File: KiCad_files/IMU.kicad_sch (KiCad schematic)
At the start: 1 part, among them U9 BNO055

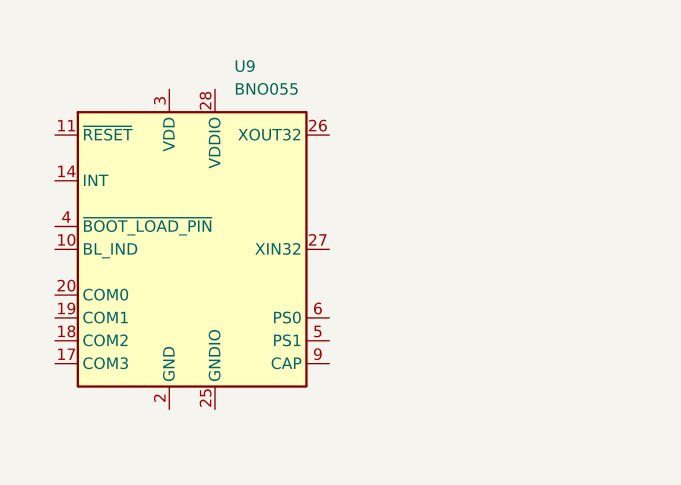
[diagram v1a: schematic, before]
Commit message: BNO085 lisätty kirjastoon
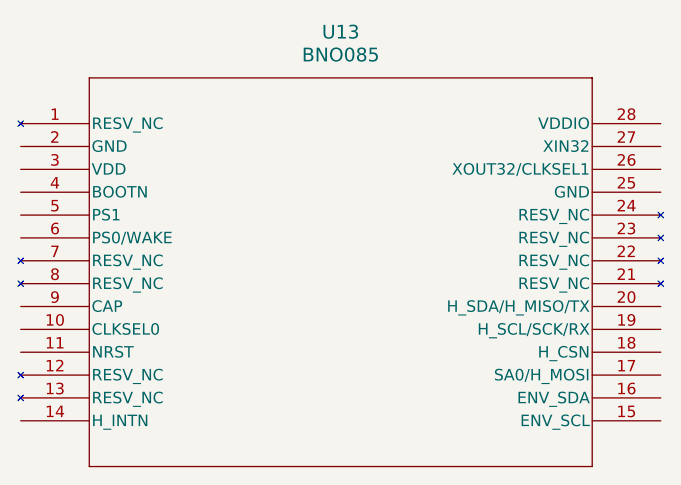
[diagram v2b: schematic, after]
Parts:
- removed U9: BNO055, Package_LGA:LGA-28_5.2x3.8mm_P0.5mm, symbol Sensor_Motion:BNO055
- added U13: BNO085, LGA-28_CEV, symbol 1_projektin osat:BNO085
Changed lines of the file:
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@@
 	(paper "A4")
 	(symbol
-		(lib_id "Sensor_Motion:BNO055")
-		(at 138.43 96.52 0)
+		(lib_id "1_projektin osat:BNO085")
+		(at 119.38 82.55 0)
 		(unit 1)
 		(exclude_from_sim no)
@@
 		(dnp no)
 		(fields_autoplaced yes)
-		(property "Reference" "U9"
-			(at 143.1133 76.2 0)
+		(property "Reference" "U13"
+			(at 154.94 72.39 0)
+			(effects
+				(font
+					(size 1.524 1.524)
+				)
+			)
+		)
+		(property "Value" "BNO085"
+			(at 154.94 74.93 0)
+			(effects
+				(font
+					(size 1.524 1.524)
+				)
+			)
+		)
+		(property "Footprint" "LGA-28_CEV"
+			(at 119.38 82.55 0)
 			(effects
 				(font
 					(size 1.27 1.27)
+					(italic yes)
 				)
-				(justify left)
+				(hide yes)
 			)
 		)
-		(property "Value" "BNO055"
-			(at 143.1133 78.74 0)
+		(property "Datasheet" "BNO085"
+			(at 119.38 82.55 0)
 			(effects
 				(font
 					(size 1.27 1.27)
+					(italic yes)
 				)
-				(justify left)
-			)
-		)
-		(property "Footprint" "Package_LGA:LGA-28_5.2x3.8mm_P0.5mm"
-			(at 144.78 113.03 0)
-			(effects
-				(font
-					(size 1.27 1.27)
-				)
-				(justify left)
 				(hide yes)
 			)
 		)
-		(property "Datasheet" "https://www.bosch-sensortec.com/media/boschsensortec/downloads/datasheets/bst-bno055-ds000.pdf"
-			(at 138.43 91.44 0)
+		(property "Description" ""
+			(at 119.38 82.55 0)
 			(effects
 				(font
@@
 			)
 		)
-		(property "Description" "Intelligent 9-axis absolute orientation sensor, LGA-28"
-			(at 138.43 96.52 0)
-			(effects
-				(font
-					(size 1.27 1.27)
-				)
-				(hide yes)
-			)
+		(pin "2"
+		)
+		(pin "1"
+		)
+		(pin "11"
+		)
+		(pin "28"
+		)
+		(pin "6"
+		)
+		(pin "4"
+		)
+		(pin "13"
 		)
 		(pin "14"
 		)
+		(pin "25"
+		)
+		(pin "5"
+		)
+		(pin "3"
+		)
+		(pin "7"
+		)
+		(pin "8"
+		)
+		(pin "9"
+		)
 		(pin "10"
 		)
-		(pin "25"
+		(pin "12"
 		)
-		(pin "11"
+		(pin "27"
 		)
-		(pin "4"
+		(pin "23"
+		)
+		(pin "24"
+		)
+		(pin "26"
+		)
+		(pin "22"
+		)
+		(pin "21"
 		)
 		(pin "20"
 		)
-		(pin "19"
+		(pin "16"
 		)
 		(pin "17"
 		)
-		(pin "1"
-		)
-		(pin "7"
-		)
-		(pin "3"
-		)
-		(pin "2"
-		)
-		(pin "8"
+		(pin "19"
 		)
 		(pin "18"
 		)
-		(pin "28"
-		)
-		(pin "9"
-		)
-		(pin "21"
-		)
-		(pin "5"
-		)
-		(pin "27"
-		)
-		(pin "26"
-		)
-		(pin "12"
-		)
-		(pin "22"
-		)
 		(pin "15"
 		)
-		(pin "6"
-		)
-		(pin "24"
-		)
-		(pin "13"
-		)
-		(pin "23"
-		)
-		(pin "16"
-		)
 		(instances
-			(project "esp"
+			(project ""
 				(path "/186d5500-054c-4b47-a89c-85f6ce2abe33/1d098c74-ef64-49cb-a95a-ee89cc8acd66"
-					(reference "U9")
+					(reference "U13")
 					(unit 1)
 				)

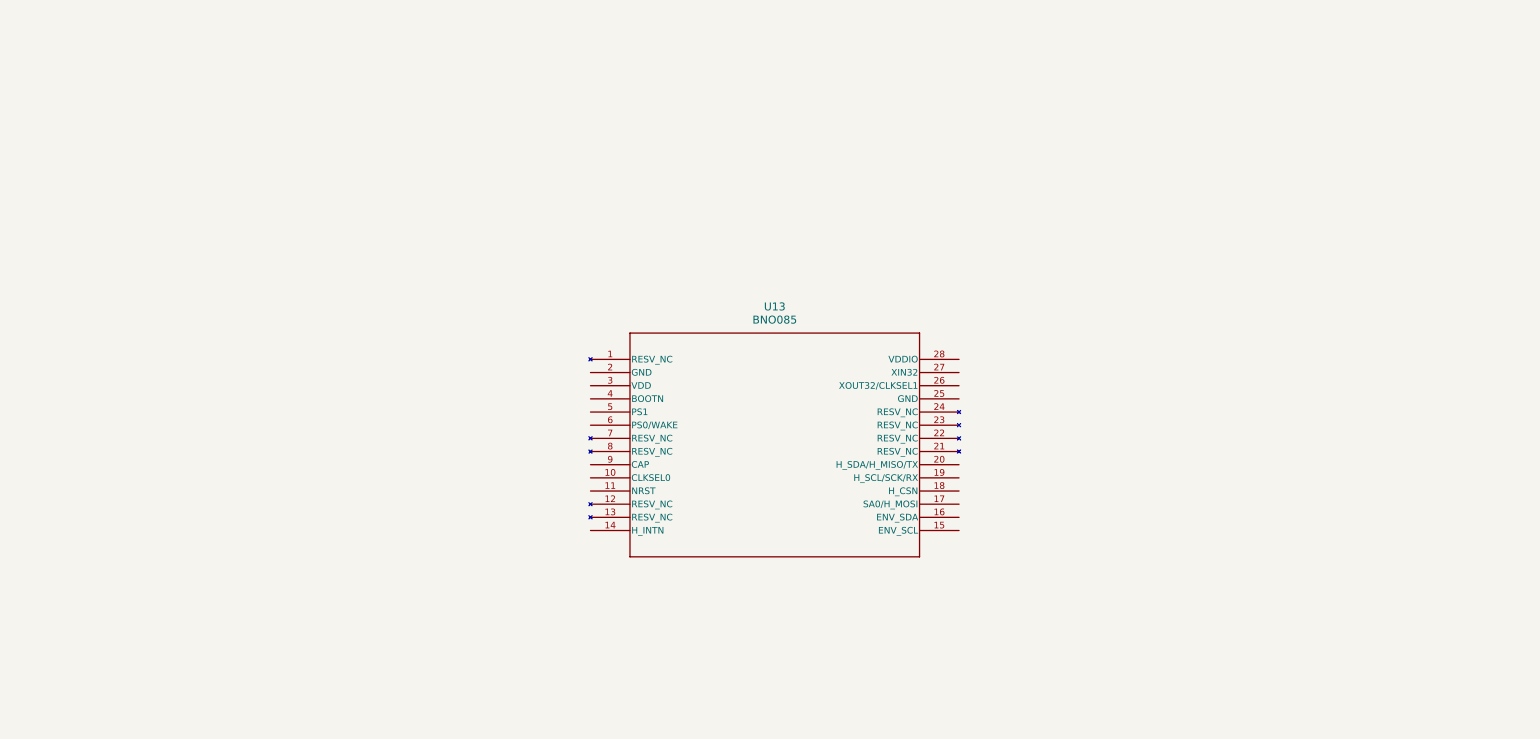
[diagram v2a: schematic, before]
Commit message: IMU schematic drawn
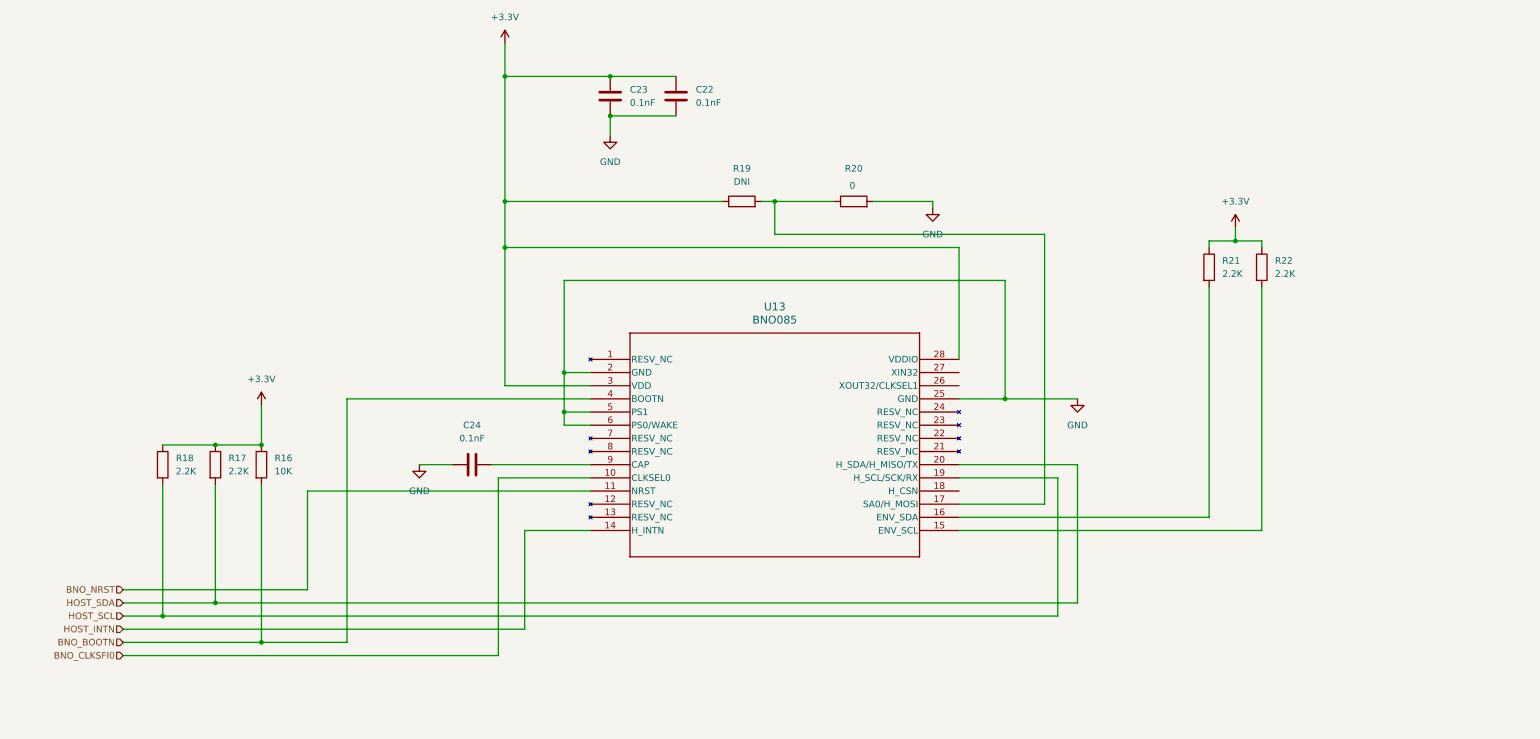
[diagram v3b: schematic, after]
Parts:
- added C22, C23, C24: 0.1nF, symbol Device:C
- added R16: 10K, symbol Device:R
- added R17, R18, R21, R22: 2.2K, symbol Device:R
- added R19: DNI, symbol Device:R
- added R20: 0, symbol Device:R
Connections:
- net BNO_CLKSFI0: now reaches U13.10 (CLKSEL0)
- net BNO_NRST: now reaches U13.11 (NRST)
- net HOST_INTN: now reaches U13.14 (H_INTN)
- net at U13.15 (ENV_SCL): now also R22.2
- net at U13.16 (ENV_SDA): now also R21.2
- net at U13.17 (SA0/H_MOSI): now also R19.2, R20.1
- net HOST_SCL: now reaches U13.19 (H_SCL/SCK/RX)
- net HOST_SCL: now also R18.2
- net GND: now reaches U13.2 (GND)
- net GND: now also U13.25 (GND), U13.5 (PS1), U13.6 (PS0/WAKE), C22.2, C23.2, C24.2, R20.2
- net HOST_SDA: now reaches U13.20 (H_SDA/H_MISO/TX)
- net HOST_SDA: now also R17.2
- net +3.3V: now reaches U13.28 (VDDIO)
- net +3.3V: now also U13.3 (VDD), C22.1, C23.1, R16.1, R17.1, R18.1, R19.1, R21.1, R22.1
- net BNO_BOOTN: now reaches U13.4 (BOOTN)
- net BNO_BOOTN: now also R16.2
- net at U13.9 (CAP): now also C24.1

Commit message: tekstiä
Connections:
- net HOST_INTN is gone; now on net BNO_BOOTN: U13.14 (H_INTN)
- net HOST_SDA is gone; now on net HOST_SCL: R17.2, U13.20 (H_SDA/H_MISO/TX)
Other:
- note added: "The BNO08X I2C interface answers to a 7-bit address of either 0x4A or 0x4B"
- note added: "i2c clock line"
- note added: "i2c data line"
- note added: "if bootn is low when reset, enter bootloader"
- note added: "interrupt line, connect to gpio with wake up capability, interrupt is active when low"
- note added: "optional secondary sensors require pulling i2c up regaardless of their presence"
- note added: "pin17 can be used to select lower bit of i2c slave address, no idea what that means"
- note added: "ps0 and ps1 are pulled to ground to select i2c"
- note added: "reset line, drive from processor or board reset"
- note added: "set lowest bit of the slave address, either low or high depending on setup"
- moved on the sheet: R21, R22

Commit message: mohloilut korjattu
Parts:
- added R23: 10K, symbol Device:R
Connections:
- net +3.3V: now also R23.1
- net BNO_BOOTN: no longer U13.14 (H_INTN)
- net BNO_CLKSFI0: now also R23.2
- net GND: now also U13.26 (XOUT32/CLKSEL1)
- net HOST_SCL: no longer R18.2, U13.20 (H_SDA/H_MISO/TX)
- new net HOST_INTN: U13.14 (H_INTN)
- new net HOST_SDA: R18.2, U13.20 (H_SDA/H_MISO/TX)
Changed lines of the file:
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@@
 	)
 	(junction
-		(at 46.99 132.08)
+		(at 55.88 147.32)
 		(diameter 0)
 		(color 0 0 0 0)
@@
 	)
 	(junction
-		(at 46.99 129.54)
-		(diameter 0)
-		(color 0 0 0 0)
-	)
-	(junction
-		(at 55.88 142.24)
-		(diameter 0)
-		(color 0 0 0 0)
-	)
-	(junction
 		(at 114.3 92.71)
 		(diameter 0)
@@
 	)
 	(junction
+		(at 46.99 137.16)
+		(diameter 0)
+		(color 0 0 0 0)
+	)
+	(junction
 		(at 36.83 132.08)
 		(diameter 0)
@@
 	)
 	(junction
-		(at 72.39 137.16)
-		(diameter 0)
-		(color 0 0 0 0)
-	)
-	(junction
 		(at 102.87 27.94)
 		(diameter 0)
@@
 	)
 	(junction
+		(at 55.88 95.25)
+		(diameter 0)
+		(color 0 0 0 0)
+	)
+	(junction
 		(at 102.87 60.96)
 		(diameter 0)
@@
 	)
 	(junction
+		(at 195.58 90.17)
+		(diameter 0)
+		(color 0 0 0 0)
+	)
+	(junction
+		(at 69.85 152.4)
+		(diameter 0)
+		(color 0 0 0 0)
+	)
+	(junction
 		(at 123.19 27.94)
 		(diameter 0)
@@
 	)
 	(junction
-		(at 55.88 137.16)
-		(diameter 0)
-		(color 0 0 0 0)
-	)
-	(junction
 		(at 243.84 100.33)
 		(diameter 0)
@@
 	(wire
 		(pts
-			(xy 46.99 129.54) (xy 213.36 129.54)
-		)
-		(stroke
-			(width 0)
-			(type default)
-		)
-	)
-	(wire
-		(pts
 			(xy 64.77 107.95) (xy 119.38 107.95)
 		)
@@
 	(wire
 		(pts
-			(xy 46.99 132.08) (xy 209.55 132.08)
+			(xy 119.38 115.57) (xy 119.38 142.24)
 		)
 		(stroke
@@
 	(wire
 		(pts
+			(xy 204.47 102.87) (xy 204.47 132.08)
+		)
+		(stroke
+			(width 0)
+			(type default)
+		)
+	)
+	(wire
+		(pts
 			(xy 207.01 110.49) (xy 190.5 110.49)
 		)
@@
 	(wire
 		(pts
+			(xy 195.58 90.17) (xy 199.39 90.17)
+		)
+		(stroke
+			(width 0)
+			(type default)
+		)
+	)
+	(wire
+		(pts
 			(xy 248.92 100.33) (xy 243.84 100.33)
 		)
@@
 	(wire
 		(pts
-			(xy 72.39 137.16) (xy 106.68 137.16)
-		)
-		(stroke
-			(width 0)
-			(type default)
-		)
-	)
-	(wire
-		(pts
 			(xy 114.3 67.31) (xy 199.39 67.31)
 		)
@@
 	(wire
 		(pts
-			(xy 55.88 91.44) (xy 55.88 99.06)
+			(xy 55.88 91.44) (xy 55.88 95.25)
 		)
 		(stroke
@@
 	(wire
 		(pts
-			(xy 36.83 132.08) (xy 46.99 132.08)
-		)
-		(stroke
-			(width 0)
-			(type default)
-		)
-	)
-	(wire
-		(pts
-			(xy 29.21 137.16) (xy 36.83 137.16)
+			(xy 55.88 106.68) (xy 55.88 147.32)
+		)
+		(stroke
+			(width 0)
+			(type default)
+		)
+	)
+	(wire
+		(pts
+			(xy 36.83 132.08) (xy 204.47 132.08)
+		)
+		(stroke
+			(width 0)
+			(type default)
+		)
+	)
+	(wire
+		(pts
+			(xy 29.21 137.16) (xy 46.99 137.16)
+		)
+		(stroke
+			(width 0)
+			(type default)
+		)
+	)
+	(wire
+		(pts
+			(xy 72.39 147.32) (xy 72.39 90.17)
 		)
 		(stroke
@@
 	(wire
 		(pts
-			(xy 106.68 115.57) (xy 119.38 115.57)
-		)
-		(stroke
-			(width 0)
-			(type default)
-		)
-	)
-	(wire
-		(pts
 			(xy 114.3 92.71) (xy 114.3 85.09)
 		)
@@
 	(wire
 		(pts
+			(xy 69.85 152.4) (xy 101.6 152.4)
+		)
+		(stroke
+			(width 0)
+			(type default)
+		)
+	)
+	(wire
+		(pts
 			(xy 101.6 152.4) (xy 101.6 105.41)
 		)
@@
 	(wire
 		(pts
+			(xy 46.99 106.68) (xy 46.99 137.16)
+		)
+		(stroke
+			(width 0)
+			(type default)
+		)
+	)
+	(wire
+		(pts
 			(xy 114.3 95.25) (xy 114.3 92.71)
 		)
@@
 	(wire
 		(pts
-			(xy 55.88 137.16) (xy 72.39 137.16)
-		)
-		(stroke
-			(width 0)
-			(type default)
-		)
-	)
-	(wire
-		(pts
 			(xy 190.5 82.55) (xy 190.5 60.96)
 		)
@@
 	(wire
 		(pts
-			(xy 213.36 102.87) (xy 213.36 129.54)
-		)
-		(stroke
-			(width 0)
-			(type default)
-		)
-	)
-	(wire
-		(pts
-			(xy 46.99 106.68) (xy 46.99 129.54)
+			(xy 190.5 87.63) (xy 195.58 87.63)
 		)
 		(stroke
@@
 	(wire
 		(pts
-			(xy 29.21 142.24) (xy 55.88 142.24)
+			(xy 46.99 137.16) (xy 209.55 137.16)
 		)
 		(stroke
@@
 	(wire
 		(pts
-			(xy 209.55 132.08) (xy 209.55 105.41)
-		)
-		(stroke
-			(width 0)
-			(type default)
-		)
-	)
-	(wire
-		(pts
-			(xy 106.68 137.16) (xy 106.68 115.57)
+			(xy 209.55 105.41) (xy 209.55 137.16)
 		)
 		(stroke
@@
 	(wire
 		(pts
-			(xy 55.88 106.68) (xy 55.88 137.16)
-		)
-		(stroke
-			(width 0)
-			(type default)
-		)
-	)
-	(wire
-		(pts
 			(xy 100.33 102.87) (xy 119.38 102.87)
 		)
@@
 	(wire
 		(pts
-			(xy 190.5 90.17) (xy 199.39 90.17)
-		)
-		(stroke
-			(width 0)
-			(type default)
-		)
-	)
-	(wire
-		(pts
-			(xy 190.5 102.87) (xy 213.36 102.87)
+			(xy 190.5 90.17) (xy 195.58 90.17)
+		)
+		(stroke
+			(width 0)
+			(type default)
+		)
+	)
+	(wire
+		(pts
+			(xy 29.21 142.24) (xy 119.38 142.24)
+		)
+		(stroke
+			(width 0)
+			(type default)
+		)
+	)
+	(wire
+		(pts
+			(xy 190.5 102.87) (xy 204.47 102.87)
+		)
+		(stroke
+			(width 0)
+			(type default)
+		)
+	)
+	(wire
+		(pts
+			(xy 55.88 95.25) (xy 62.23 95.25)
 		)
 		(stroke
@@
 	(wire
 		(pts
-			(xy 46.99 132.08) (xy 46.99 129.54)
-		)
-		(stroke
-			(width 0)
-			(type default)
-		)
-	)
-	(wire
-		(pts
-			(xy 29.21 152.4) (xy 101.6 152.4)
-		)
-		(stroke
-			(width 0)
-			(type default)
-		)
-	)
-	(wire
-		(pts
-			(xy 55.88 142.24) (xy 55.88 137.16)
+			(xy 29.21 152.4) (xy 69.85 152.4)
 		)
 		(stroke
@@
 	(wire
 		(pts
-			(xy 36.83 137.16) (xy 36.83 132.08)
+			(xy 55.88 147.32) (xy 72.39 147.32)
+		)
+		(stroke
+			(width 0)
+			(type default)
+		)
+	)
+	(wire
+		(pts
+			(xy 69.85 95.25) (xy 69.85 152.4)
 		)
 		(stroke
@@
 	(wire
 		(pts
-			(xy 55.88 147.32) (xy 55.88 142.24)
-		)
-		(stroke
-			(width 0)
-			(type default)
-		)
-	)
-	(wire
-		(pts
-			(xy 72.39 137.16) (xy 72.39 90.17)
+			(xy 55.88 95.25) (xy 55.88 99.06)
+		)
+		(stroke
+			(width 0)
+			(type default)
+		)
+	)
+	(wire
+		(pts
+			(xy 195.58 87.63) (xy 195.58 90.17)
 		)
 		(stroke
@@
 					(unit 1)
 				)
+			)
+		)
+	)
+	(symbol
+		(lib_id "Device:R")
+		(at 66.04 95.25 90)
+		(unit 1)
+		(exclude_from_sim no)
+		(in_bom yes)
+		(on_board yes)
+		(dnp no)
+		(fields_autoplaced yes)
+		(property "Reference" "R23"
+			(at 66.04 88.9 90)
+			(effects
+				(font
+					(size 1.27 1.27)
+				)
+			)
+		)
+		(property "Value" "10K"
+			(at 66.04 91.44 90)
+			(effects
+				(font
+					(size 1.27 1.27)
+				)
+			)
+		)
+		(property "Footprint" ""
+			(at 66.04 97.028 90)
+			(effects
+				(font
+					(size 1.27 1.27)
+				)
+				(hide yes)
+			)
+		)
+		(property "Datasheet" "~"
+			(at 66.04 95.25 0)
+			(effects
+				(font
+					(size 1.27 1.27)
+				)
+				(hide yes)
+			)
+		)
+		(property "Description" "Resistor"
+			(at 66.04 95.25 0)
+			(effects
+				(font
+					(size 1.27 1.27)
+				)
+				(hide yes)
+			)
+		)
+		(pin "1"
+		)
+		(pin "2"
+		)
+		(instances
+			(project "esp"
+				(path "/186d5500-054c-4b47-a89c-85f6ce2abe33/1d098c74-ef64-49cb-a95a-ee89cc8acd66"
+					(reference "R23")
+					(unit 1)
+				)

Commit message: footprinttejä
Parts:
- U13: footprint LGA-28_CEV -> 1_project_library:BNO085
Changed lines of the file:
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@@
 			)
 		)
-		(property "Footprint" "LGA-28_CEV"
+		(property "Footprint" "1_project_library:BNO085"
 			(at 119.38 82.55 0)
 			(effects
